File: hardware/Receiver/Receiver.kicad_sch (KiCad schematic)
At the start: 99 parts, among them IC1 ESP32-C3-MINI-1-N4, J1 USB_C_Receptacle_USB2.0, J2 UP_BTN, J3 DN_BTN, J3 UART, J4 Conn_01x03, J6 Conn_01x04, Q1 2N7002, SW1 Reset, SW2 SW_Push, U1 DMG6602SVTQ, U1 TPS22810DRV, U2 DMG6602SVTQ, U2 TPS22810DRV, U3 AZ1117-3.3, U3 TLV493DA1B6HTSA2

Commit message: Completed Receiver PCB
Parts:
- removed J2: UP_BTN, Connector_JST:JST_PH_B2B-PH-K_1x02_P2.00mm_Vertical, symbol Connector_Generic:Conn_01x02
- removed J3: DN_BTN, Connector_JST:JST_PH_B2B-PH-K_1x02_P2.00mm_Vertical, symbol Connector_Generic:Conn_01x02
- removed R14, R9: 100k, Capacitor_SMD:C_0402_1005Metric, symbol Device:R_Small
- added H5 (x3): MountingHole, MountingHole:MountingHole_3.2mm_M3_DIN965_Pad_TopBottom, symbol Mechanical:MountingHole
- H1, H2, H3, H4, H5: footprint MountingHole:MountingHole_2.2mm_M2 -> MountingHole:MountingHole_3.2mm_M3_DIN965_Pad_TopBottom
- IC1: footprint ESP32C3MINI1N4:ESP32C3MINI1N4 -> ESP32MINI1N4:ESP32MINI1N4
- J1: footprint footprints:CONN_GSB1CA11101DSHR_AMP -> Connector_USB:USB_C_Receptacle_JAE_DX07S016JA1R1500
- J3: value UART -> 20021511-00006T4LF
- SW2: value SW_Push -> 1825027-8; footprint Connector_PinSocket_2.54mm:PinSocket_1x02_P2.54mm_Horizontal -> Button_THT:SW2_1825027-C_TEC
- U3: footprint AZ1117:SOT223 -> Package_TO_SOT_SMD:SOT-223
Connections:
- net MS1: now also IC1.7 (I39); no longer IC1.5 (I37)
- net MS3: now also IC1.5 (I37); no longer IC1.7 (I39)
- net OUT1B: now reaches A1.21 (OUT1B), J6.1 (Pin_1)
- net OUT1A: now reaches A1.24 (OUT1A), J6.2 (Pin_2)
- net OUT2A: now reaches A1.26 (OUT2A), J6.3 (Pin_3)
- net OUT2B: now reaches A1.1 (OUT2B), J6.4 (Pin_4)

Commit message: Removed old files
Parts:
- added J6: JST_PH, Connector_JST:JST_PH_B6B-PH-K_1x06_P2.00mm_Vertical, symbol Connector_Generic:Conn_01x06
- added Q10, Q11, Q2, Q3, Q4, Q8, Q9: NChan, Package_TO_SOT_SMD:SOT-23, symbol Transistor_FET:DMG3418L
- added Q5, Q6, Q7: PChan, Package_TO_SOT_SMD:SOT-23, symbol Transistor_FET:BSS83P
- added R21, R22, R23, R24, R25, R26, R28, R30, R32: 100k, Resistor_SMD:R_0402_1005Metric, symbol Device:R_Small
- added R27: 282k, Resistor_SMD:R_0402_1005Metric, symbol Device:R_Small
- added R29: 155k, Resistor_SMD:R_0402_1005Metric, symbol Device:R_Small
- added R31: 28k, Resistor_SMD:R_0402_1005Metric, symbol Device:R_Small
- added R33, R34, R35, R36: 400, Resistor_SMD:R_2010_5025Metric, symbol Device:R_Small
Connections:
- net GND: now also J6.1 (Pin_1), Q11.2 (S), Q2.2 (S), Q3.2 (S), Q4.2 (S), R21.2, R22.2, R23.2, R28.2, R30.2, R32.2
- new net: Q10.3 (D), R35.2
- new net: Q3.3 (D), Q6.1 (G), R25.2
- new net: Q5.2 (S), R27.1
- new net: Q8.3 (D), R33.2
- new net: Q2.3 (D), Q5.1 (G), R24.2
- new net: Q11.3 (D), R36.2
- new net: Q6.2 (S), R29.1
- new net: Q9.3 (D), R34.2
- new net: Q4.3 (D), Q7.1 (G), R26.2
- new net: Q7.2 (S), R31.1
- new net BAT_+: J6.5 (Pin_5), R33.1
- new net BAT_A: J6.4 (Pin_4), Q5.3 (D), Q8.2 (S), R24.1, R34.1
- new net BAT_B: J6.3 (Pin_3), Q6.3 (D), Q9.2 (S), R25.1, R35.1
- new net BAT_C: J6.2 (Pin_2), Q10.2 (S), Q7.3 (D), R26.1, R36.1
- new net C1: Q8.1 (G)
- new net C2: Q9.1 (G)
- new net C3: Q10.1 (G)
- new net C4: Q11.1 (G)
- new net M2: Q2.1 (G), R21.1
- new net M3: Q3.1 (G), R22.1
- new net M4: Q4.1 (G), R23.1
- new net S2: R27.2, R28.1
- new net S3: R29.2, R30.1
- new net S4: R31.2, R32.1
- new net TC: J6.6 (Pin_6)

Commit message: Revision 1.2 of receiver board
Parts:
- removed C15: 0.1u, Capacitor_SMD:C_0402_1005Metric, symbol Device:C
- removed J6: JST_PH, Connector_JST:JST_PH_B6B-PH-K_1x06_P2.00mm_Vertical, symbol Connector_Generic:Conn_01x06
- removed Q10, Q11, Q2, Q3, Q4, Q8, Q9: NChan, Package_TO_SOT_SMD:SOT-23, symbol Transistor_FET:DMG3418L
- removed Q5, Q6, Q7: PChan, Package_TO_SOT_SMD:SOT-23, symbol Transistor_FET:BSS83P
- removed R21, R22, R23, R24, R25, R26, R28, R30, R32: 100k, Resistor_SMD:R_0402_1005Metric, symbol Device:R_Small
- removed R27: 282k, Resistor_SMD:R_0402_1005Metric, symbol Device:R_Small
- removed R29: 155k, Resistor_SMD:R_0402_1005Metric, symbol Device:R_Small
- removed R31: 28k, Resistor_SMD:R_0402_1005Metric, symbol Device:R_Small
- removed R33, R34, R35, R36: 400, Resistor_SMD:R_2010_5025Metric, symbol Device:R_Small
- D3: value D_Schottky -> EVVO SS16; footprint Diode_SMD:D_SOD-128 -> Diode_SMD:D_SMA
- D3: value D -> 1N4148WQ-13-F; footprint Capacitor_SMD:C_0402_1005Metric -> Diode_SMD:D_SOD-123
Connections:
- net DN_BTN is gone; now on net SHUTDOWN: IC1.10 (I35)
- net UP_BTN is gone; now on net ADDRS_LED: IC1.9 (I34)
- net ADDRS_LED: no longer IC1.34 (IO21)
- net DIR: now also IC1.11 (IO32); no longer IC1.29 (IO5)
- net MOT_nRST: now also IC1.13 (IO25); no longer IC1.26 (IO10)
- net MS1: now also IC1.16 (IO14); no longer IC1.7 (I39)
- net MS2: now also IC1.15 (IO27); no longer IC1.6 (I38)
- net MS3: now also IC1.14 (IO26); no longer IC1.5 (I37)
- net STEP: now also IC1.12 (IO33); no longer IC1.25 (IO9)
- no-connect marks 29 -> 27
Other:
- moved on the sheet: SW1

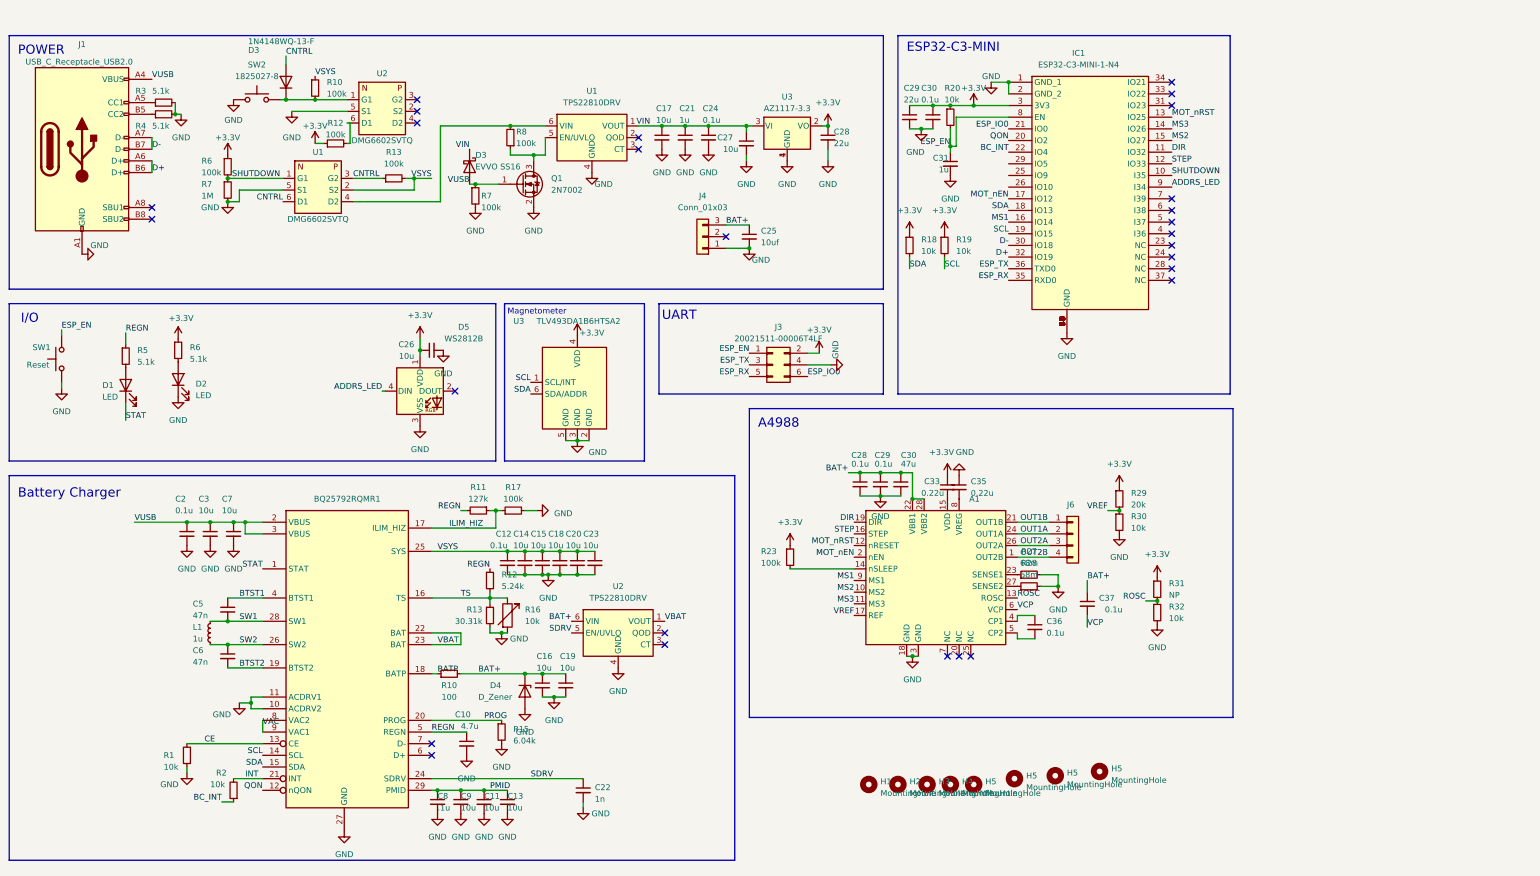
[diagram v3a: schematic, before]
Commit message: Add bms to schematic
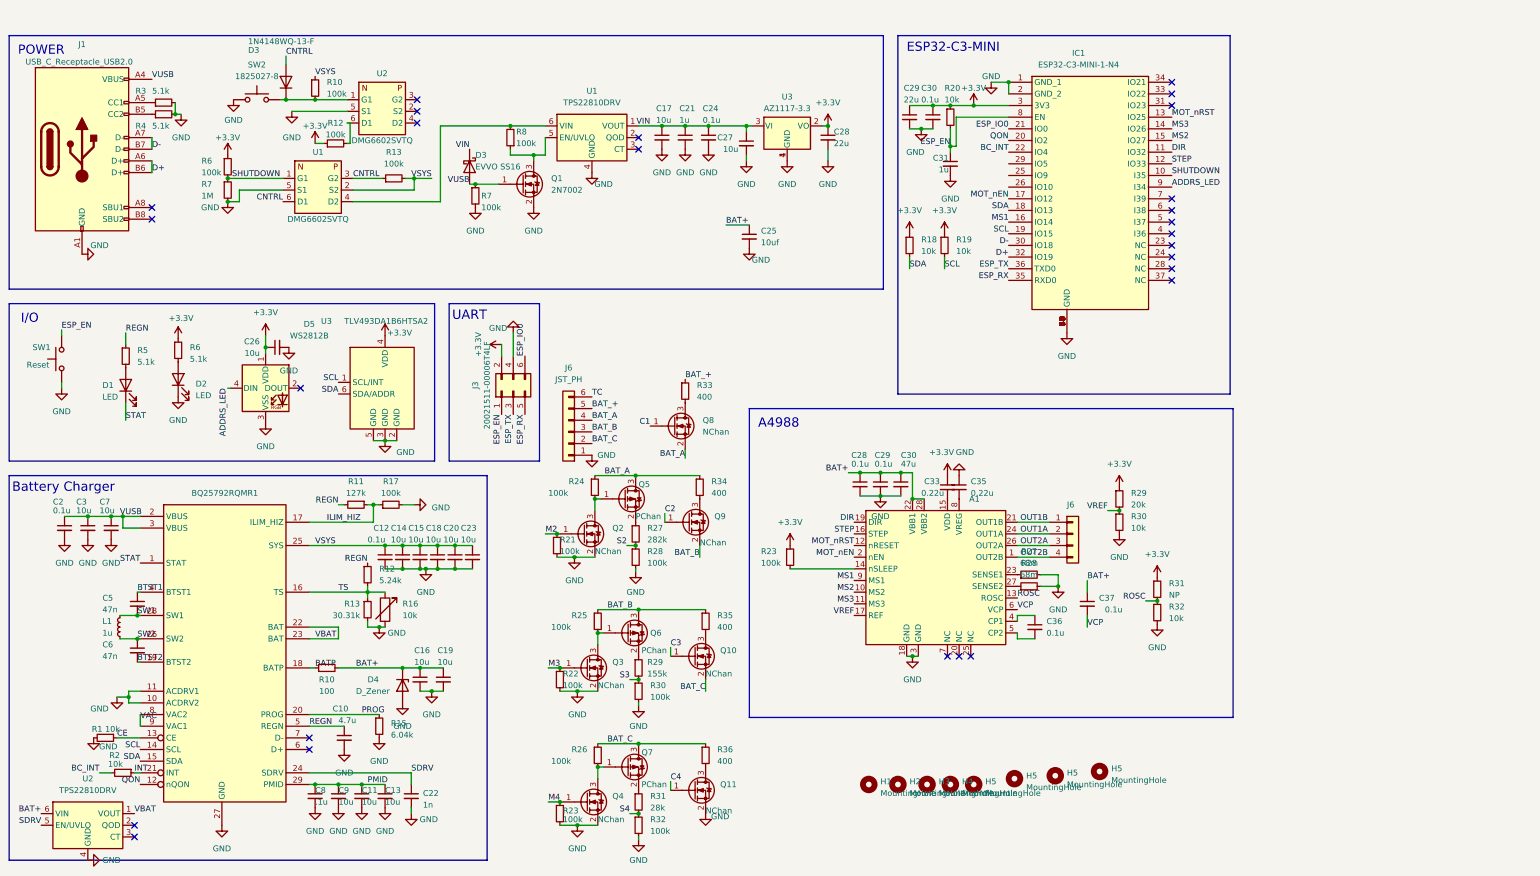
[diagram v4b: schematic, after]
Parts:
- removed J4: Conn_01x03, Connector_JST:JST_PH_B3B-PH-K_1x03_P2.00mm_Vertical, symbol Connector_Generic:Conn_01x03
- added J6: JST_PH, Connector_JST:JST_PH_B6B-PH-K_1x06_P2.00mm_Vertical, symbol Connector_Generic:Conn_01x06
- added Q10, Q11, Q2, Q3, Q4, Q8, Q9: NChan, Package_TO_SOT_SMD:SOT-23, symbol Transistor_FET:DMG3418L
- added Q5, Q6, Q7: PChan, Package_TO_SOT_SMD:SOT-23, symbol Transistor_FET:BSS83P
- added R21, R22, R23, R24, R25, R26, R28, R30, R32: 100k, Resistor_SMD:R_0402_1005Metric, symbol Device:R_Small
- added R27: 282k, Resistor_SMD:R_0402_1005Metric, symbol Device:R_Small
- added R29: 155k, Resistor_SMD:R_0402_1005Metric, symbol Device:R_Small
- added R31: 28k, Resistor_SMD:R_0402_1005Metric, symbol Device:R_Small
- added R33, R34, R35, R36: 400, Resistor_SMD:R_2010_5025Metric, symbol Device:R_Small
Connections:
- net BC_INT: now also R2.2; no longer R2.1
- net CE: now also R1.1; no longer R1.2
- net GND: now also R1.2, J6.1 (Pin_1), Q11.2 (S), Q2.2 (S), Q3.2 (S), Q4.2 (S), R21.2, R22.2, R23.2, R28.2, R30.2, R32.2; no longer R1.1
- net INT: now also R2.1; no longer R2.2
- new net: Q4.3 (D), Q7.1 (G), R26.2
- new net: Q6.2 (S), R29.1
- new net: Q5.2 (S), R27.1
- new net: Q8.3 (D), R33.2
- new net: Q3.3 (D), Q6.1 (G), R25.2
- new net: Q2.3 (D), Q5.1 (G), R24.2
- new net: Q11.3 (D), R36.2
- new net: Q7.2 (S), R31.1
- new net: Q9.3 (D), R34.2
- new net: Q10.3 (D), R35.2
- new net BAT_+: J6.5 (Pin_5), R33.1
- new net BAT_A: J6.4 (Pin_4), Q5.3 (D), Q8.2 (S), R24.1, R34.1
- new net BAT_B: J6.3 (Pin_3), Q6.3 (D), Q9.2 (S), R25.1, R35.1
- new net BAT_C: J6.2 (Pin_2), Q10.2 (S), Q7.3 (D), R26.1, R36.1
- new net C1: Q8.1 (G)
- new net C2: Q9.1 (G)
- new net C3: Q10.1 (G)
- new net C4: Q11.1 (G)
- new net M2: Q2.1 (G), R21.1
- new net M3: Q3.1 (G), R22.1
- new net M4: Q4.1 (G), R23.1
- new net S2: R27.2, R28.1
- new net S3: R29.2, R30.1
- new net S4: R31.2, R32.1
- new net TC: J6.6 (Pin_6)
- no-connect marks 27 -> 26
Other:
- note removed: "Magnetometer"
- moved on the sheet: BQ25792RQMR1, C10, C11, C12, C13, C14, C15, C16, C18, C19, C2, C20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

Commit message: BMS added to hardware
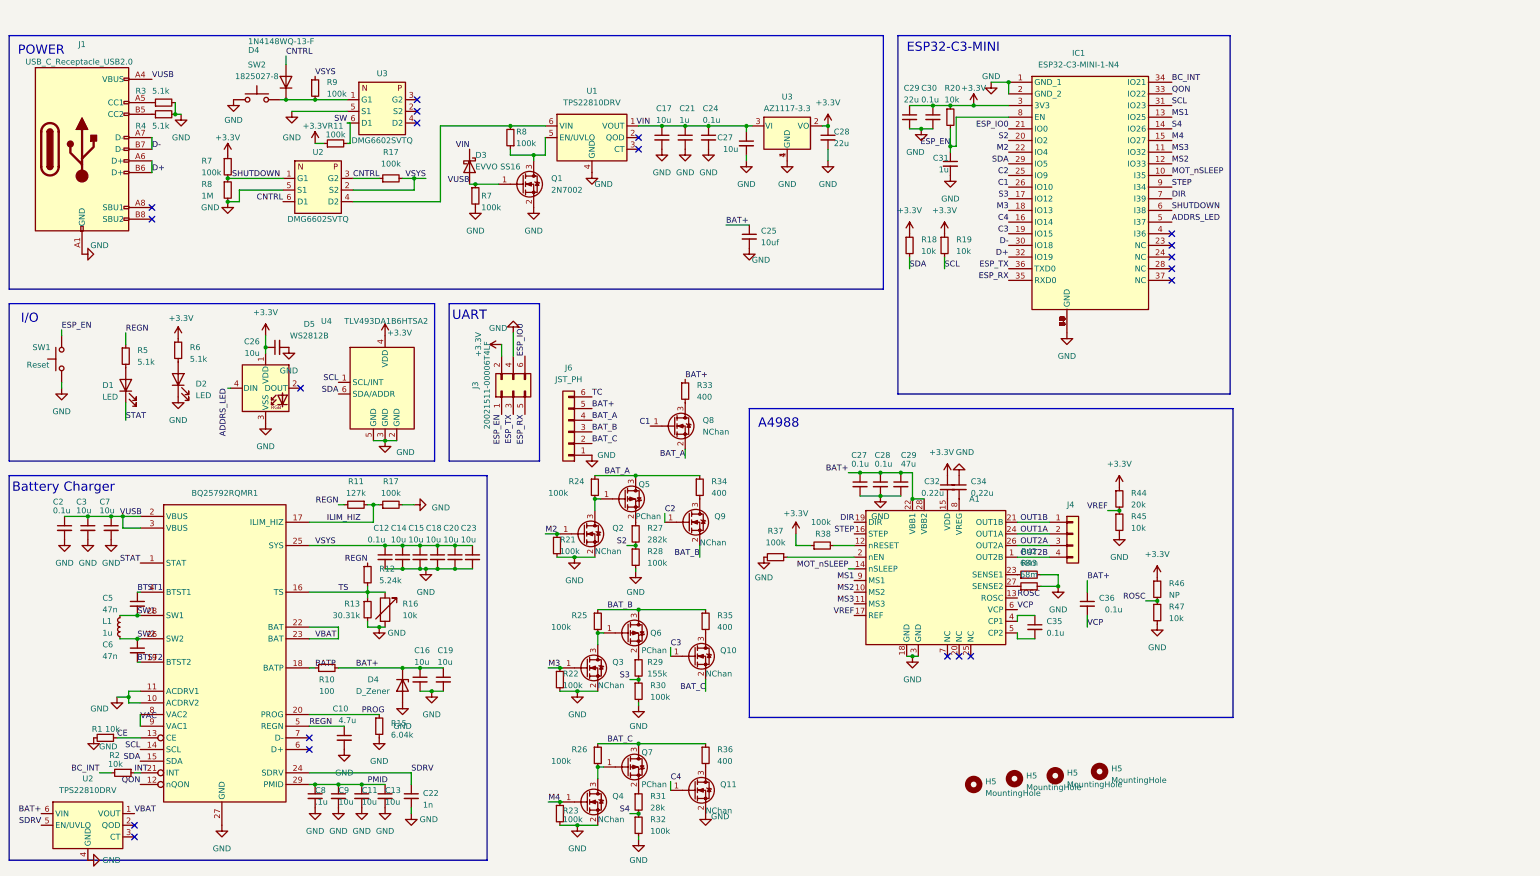
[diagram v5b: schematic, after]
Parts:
- removed H1, H2, H3, H4: MountingHole, MountingHole:MountingHole_3.2mm_M3_DIN965_Pad_TopBottom, symbol Mechanical:MountingHole
- removed R23: 100k, Resistor_SMD:R_0402_1005Metric, symbol Device:R_Small
- added R37, R38: 100k, Resistor_SMD:R_0402_1005Metric, symbol Device:R_Small
- renumbered C28 to C27, C29 to C28, C30 to C29, C33 to C32, C35 to C34, C36 to C35, C37 to C36, D3 to D4, J6 to J4, R12 to R11, R13 to R17, R27 to R42, R28 to R43, R29 to R44, R30 to R45, R31 to R46, R32 to R47, R6 to R7, R7 to R8, R10 to R9, U1 to U2, U2 to U3, U3 to U4
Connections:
- net BAT_+ is gone; now on net BAT+: J6.5 (Pin_5), R33.1
- net +3.3V: now also R38.1
- net ADDRS_LED: now also IC1.5 (I37); no longer IC1.9 (I34)
- net BC_INT: now also IC1.34 (IO21); no longer IC1.22 (IO4)
- net C1: now also IC1.26 (IO10)
- net C2: now also IC1.25 (IO9)
- net C3: now also IC1.19 (IO15)
- net C4: now also IC1.16 (IO14)
- net DIR: now also IC1.7 (I39); no longer IC1.11 (IO32)
- net GND: now also R37.2
- net M2: now also IC1.22 (IO4)
- net M3: now also IC1.18 (IO13)
- net M4: now also IC1.15 (IO27)
- net MS1: now also IC1.13 (IO25); no longer IC1.16 (IO14)
- net MS2: now also IC1.12 (IO33); no longer IC1.15 (IO27)
- net MS3: now also IC1.11 (IO32); no longer IC1.14 (IO26)
- net QON: now also IC1.33 (IO22); no longer IC1.20 (IO2)
- net S2: now also IC1.20 (IO2)
- net S3: now also IC1.17 (IO12)
- net S4: now also IC1.14 (IO26)
- net SCL: now also IC1.31 (IO23); no longer IC1.19 (IO15)
- net SDA: now also IC1.29 (IO5); no longer IC1.18 (IO13)
- net SHUTDOWN: now also IC1.6 (I38); no longer IC1.10 (I35)
- net STEP: now also IC1.9 (I34); no longer IC1.12 (IO33)
- net MOT_nSLEEP: now reaches A1.14 (nSLEEP)
- net MOT_nSLEEP: now also IC1.10 (I35)
- net SW: now reaches R11.2, U3.6 (D1)
- net MOT_nEN: no longer names the net of A1.2 (nEN)
- net MOT_nEN: now also R37.1; no longer IC1.17 (IO12)
- net MOT_nRST: no longer names the net of A1.12 (nRESET)
- net MOT_nRST: now also R38.2; no longer IC1.13 (IO25)
- no-connect marks 26 -> 20
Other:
- moved on the sheet: R17
